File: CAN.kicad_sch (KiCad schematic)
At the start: 0 parts

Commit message: Latest updates
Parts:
- added C16: 100n, symbol Device:C
- added J7, J8: 8P8C_Shielded, symbol Connector:8P8C_Shielded
- added R8: 10k, symbol Device:R
- added R9: 120, symbol Device:R
- added SW2: SW_DIP_x01, symbol Switch:SW_DIP_x01
- added U2: SIT65HVD230DR, EasyEDA:SOP-8_L4.9-W3.9-P1.27-LS6.0-BL, symbol EasyEDA:SIT65HVD230DR
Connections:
- new net: R8.1, U2.8 (RS)
- new net: R9.1, SW2.1
- new net +3.3V: C16.1, U2.3 (VCC)
- new net CAN_H: J7.1, J8.1, SW2.2, U2.7 (CANH)
- new net CAN_L: J7.2, J8.2, R9.2, U2.6 (CANL)
- new net CAN_RXD: U2.4 (R)
- new net CAN_TXD: U2.1 (D)
- new net Earth: J7.SH, J8.SH
- new net GND: C16.2, J7.3, J8.3, R8.2, U2.2 (GND)
- no-connect marks 0 -> 11
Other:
- note added: "RS pulldown can be 0Ohm or 10-100Kohm depending on speed mode required"
- note added: "Two RJ45 Connectors are here to support daisy chaining out of the box when needed"

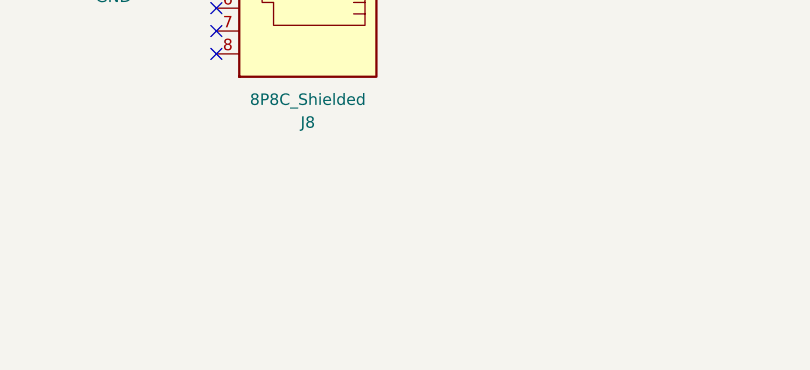
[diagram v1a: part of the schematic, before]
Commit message: Latest changes (added SD , USB , CAN , RS485)
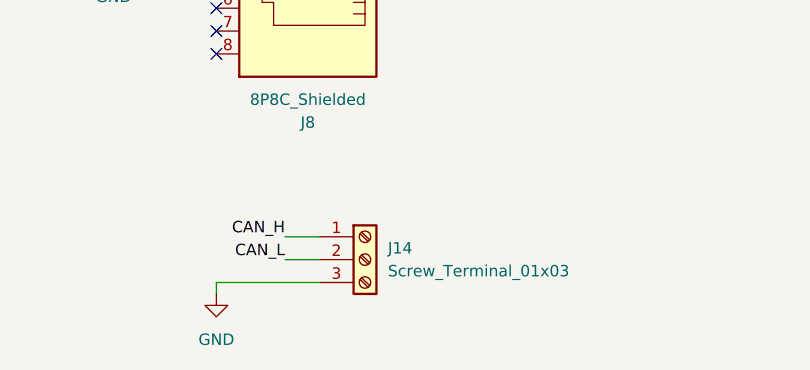
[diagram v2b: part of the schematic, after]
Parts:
- added J14: Screw_Terminal_01x03, TerminalBlock_Phoenix:TerminalBlock_Phoenix_PT-1,5-3-3.5-H_1x03_P3.50mm_Horizontal, symbol Connector:Screw_Terminal_01x03
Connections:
- net CAN_H: now also J14.1 (Pin_1)
- net CAN_L: now also J14.2 (Pin_2)
- net GND: now also J14.3 (Pin_3)
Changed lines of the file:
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@@
+	(wire
+		(pts
+			(xy 215.9 143.51) (xy 219.71 143.51)
+		)
+		(stroke
+			(width 0)
+			(type default)
+		)
+	)
 	(wire
 		(pts
@@
 	(wire
 		(pts
+			(xy 208.28 149.86) (xy 208.28 148.59)
+		)
+		(stroke
+			(width 0)
+			(type default)
+		)
+	)
+	(wire
+		(pts
 			(xy 196.85 77.47) (xy 196.85 76.2)
 		)
@@
 	(wire
 		(pts
+			(xy 215.9 146.05) (xy 219.71 146.05)
+		)
+		(stroke
+			(width 0)
+			(type default)
+		)
+	)
+	(wire
+		(pts
 			(xy 218.44 62.23) (xy 218.44 66.04)
 		)
@@
 		(pts
 			(xy 236.22 104.14) (xy 236.22 97.79)
+		)
+		(stroke
+			(width 0)
+			(type default)
+		)
+	)
+	(wire
+		(pts
+			(xy 208.28 148.59) (xy 219.71 148.59)
 		)
 		(stroke
@@
 	)
 	(label "CAN_H"
+		(at 215.9 143.51 180)
+		(effects
+			(font
+				(size 1.27 1.27)
+			)
+			(justify right bottom)
+		)
+	)
+	(label "CAN_H"
 		(at 125.73 74.93 0)
 		(effects
@@
 	(label "CAN_H"
 		(at 204.47 105.41 180)
+		(effects
+			(font
+				(size 1.27 1.27)
+			)
+			(justify right bottom)
+		)
+	)
+	(label "CAN_L"
+		(at 215.9 146.05 180)
 		(effects
 			(font
@@
 					(unit 1)
 				)
+			)
+		)
+	)
+	(symbol
+		(lib_id "power:GND")
+		(at 208.28 149.86 0)
+		(unit 1)
+		(exclude_from_sim no)
+		(in_bom yes)
+		(on_board yes)
+		(dnp no)
+		(fields_autoplaced yes)
+		(property "Reference" "#PWR061"
+			(at 208.28 156.21 0)
+			(effects
+				(font
+					(size 1.27 1.27)
+				)
+				(hide yes)
+			)
+		)
+		(property "Value" "GND"
+			(at 208.28 154.94 0)
+			(effects
+				(font
+					(size 1.27 1.27)
+				)
+			)
+		)
+		(property "Footprint" ""
+			(at 208.28 149.86 0)
+			(effects
+				(font
+					(size 1.27 1.27)
+				)
+				(hide yes)
+			)
+		)
+		(property "Datasheet" ""
+			(at 208.28 149.86 0)
+			(effects
+				(font
+					(size 1.27 1.27)
+				)
+				(hide yes)
+			)
+		)
+		(property "Description" "Power symbol creates a global label with name \"GND\" , ground"
+			(at 208.28 149.86 0)
+			(effects
+				(font
+					(size 1.27 1.27)
+				)
+				(hide yes)
+			)
+		)
+		(pin "1"
+		)
+		(instances
+			(project "OhWare"
+				(path "/38f33acd-ac87-4918-9c1f-d78977d10c9f/1b0ef705-9879-4141-ae37-7f2caae893a3"
+					(reference "#PWR061")
+					(unit 1)
+				)
+			)
+		)
+	)
+	(symbol
+		(lib_id "Connector:Screw_Terminal_01x03")
+		(at 224.79 146.05 0)
+		(unit 1)
+		(exclude_from_sim no)
+		(in_bom yes)
+		(on_board yes)
+		(dnp no)
+		(fields_autoplaced yes)
+		(property "Reference" "J14"
+			(at 227.33 144.7799 0)
+			(effects
+				(font
+					(size 1.27 1.27)
+				)
+				(justify left)
+			)
+		)
+		(property "Value" "Screw_Terminal_01x03"
+			(at 227.33 147.3199 0)
+			(effects
+				(font
+					(size 1.27 1.27)
+				)
+				(justify left)
+			)
+		)
+		(property "Footprint" "TerminalBlock_Phoenix:TerminalBlock_Phoenix_PT-1,5-3-3.5-H_1x03_P3.50mm_Horizontal"
+			(at 224.79 146.05 0)
+			(effects
+				(font
+					(size 1.27 1.27)
+				)
+				(hide yes)
+			)
+		)
+		(property "Datasheet" "~"
+			(at 224.79 146.05 0)
+			(effects
+				(font
+					(size 1.27 1.27)
+				)
+				(hide yes)
+			)
+		)
+		(property "Description" "Generic screw terminal, single row, 01x03, script generated (kicad-library-utils/schlib/autogen/connector/)"
+			(at 224.79 146.05 0)
+			(effects
+				(font
+					(size 1.27 1.27)
+				)
+				(hide yes)
+			)
+		)
+		(pin "2"
+		)
+		(pin "1"
+		)
+		(pin "3"
+		)
+		(instances
+			(project ""
+				(path "/38f33acd-ac87-4918-9c1f-d78977d10c9f/1b0ef705-9879-4141-ae37-7f2caae893a3"
+					(reference "J14")
+					(unit 1)
+				)

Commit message: Schematic--Footprint link
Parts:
- C16: footprint (none) -> Capacitor_SMD:C_0805_2012Metric
- J7, J8: footprint (none) -> Connector_RJ:RJ45_Ninigi_GE
- R8, R9: footprint (none) -> Resistor_SMD:R_0805_2012Metric
- SW2: footprint (none) -> Button_Switch_THT:SW_DIP_SPSTx01_Slide_6.7x4.1mm_W7.62mm_P2.54mm_LowProfile
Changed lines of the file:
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@@
 			)
 		)
-		(property "Footprint" ""
+		(property "Footprint" "Connector_RJ:RJ45_Ninigi_GE"
 			(at 218.44 79.375 90)
 			(effects
@@
 			)
 		)
-		(property "Footprint" ""
+		(property "Footprint" "Resistor_SMD:R_0805_2012Metric"
 			(at 165.862 85.09 90)
 			(effects
@@
 			)
 		)
-		(property "Footprint" ""
+		(property "Footprint" "Capacitor_SMD:C_0805_2012Metric"
 			(at 77.1652 85.09 0)
 			(effects
@@
 			)
 		)
-		(property "Footprint" ""
+		(property "Footprint" "Connector_RJ:RJ45_Ninigi_GE"
 			(at 218.44 113.665 90)
 			(effects
@@
 		(on_board yes)
 		(dnp no)
-		(fields_autoplaced yes)
 		(property "Reference" "SW2"
 			(at 171.45 72.3899 90)
@@
 			)
 		)
-		(property "Footprint" ""
-			(at 167.64 73.66 0)
+		(property "Footprint" "Button_Switch_THT:SW_DIP_SPSTx01_Slide_6.7x4.1mm_W7.62mm_P2.54mm_LowProfile"
+			(at 154.94 73.66 0)
 			(effects
 				(font
@@
 			)
 		)
-		(property "Footprint" ""
+		(property "Footprint" "Resistor_SMD:R_0805_2012Metric"
 			(at 140.462 78.74 90)
 			(effects
